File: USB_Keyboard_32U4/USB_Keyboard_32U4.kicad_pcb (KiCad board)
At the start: 2 copper layers, 13.4 x 24.2 mm, 12 parts, among them J1 USB_C_Receptacle_USB2.0_16P, U1 ATmega32U4-A, Y1 16mhz

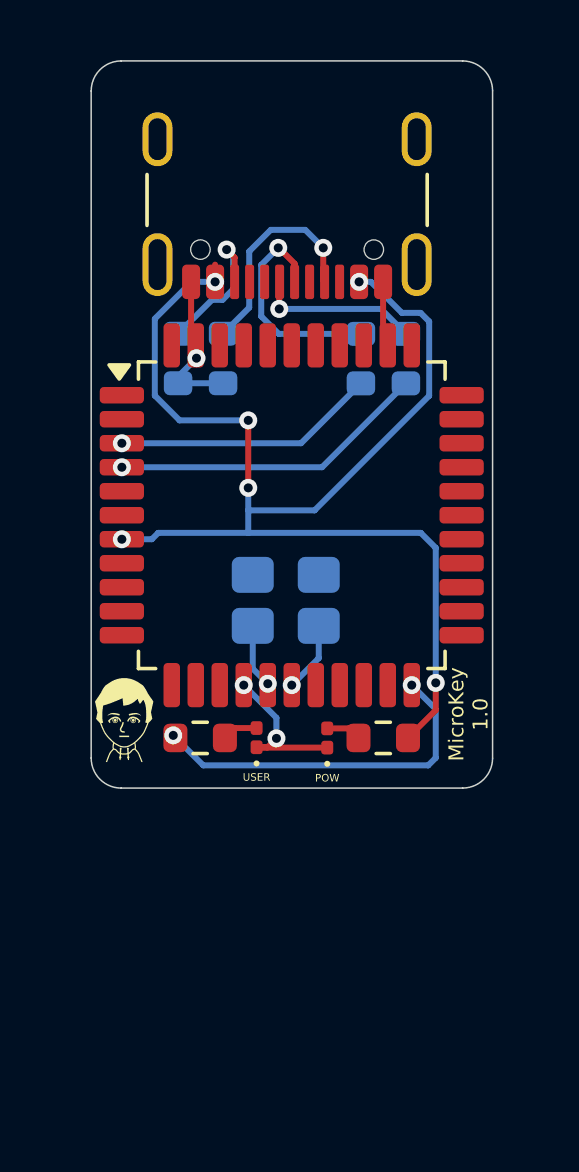
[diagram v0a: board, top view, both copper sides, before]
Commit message: Update keyboard PCB footprints to 0805
This commit updates the USB keyboard board from 0201/0603 passive packages to 0805 hand-solder footprints for the LEDs and resistors. It repositions the affected components, refreshes the KiCad project metadata, and adjusts the board outline and routed tracks to match the larger parts. It also includes the generated production .DS_Store artifact.
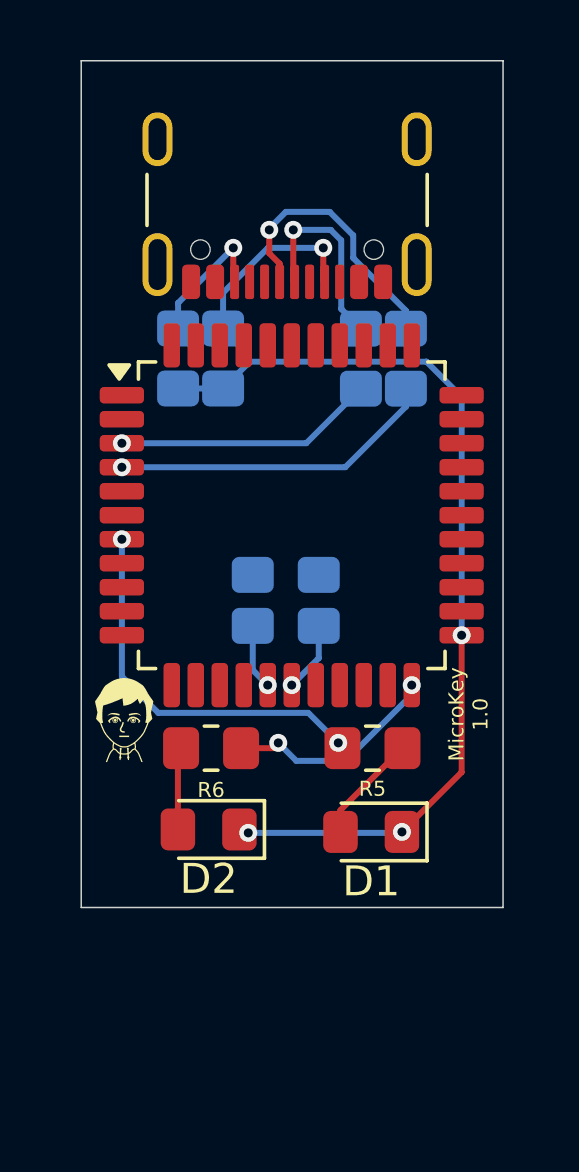
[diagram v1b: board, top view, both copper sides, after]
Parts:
- D1: renamed from POW; value LED -> RED; footprint LED_SMD:LED_0201_0603Metric -> LED_SMD:LED_0805_2012Metric_Pad1.15x1.40mm_HandSolder
- D2: renamed from USER; value LED -> BLUE; footprint LED_SMD:LED_0201_0603Metric -> LED_SMD:LED_0805_2012Metric_Pad1.15x1.40mm_HandSolder
- R1, R2, R3, R4, R5, R6: footprint Resistor_SMD:R_0603_1608Metric -> Resistor_SMD:R_0805_2012Metric_Pad1.20x1.40mm_HandSolder
- moved D1 3.46 mm to (122.6, 92.0), turned to 180 degrees
- moved D2 3.45 mm to (117.2, 91.9), turned to 180 degrees
- moved R6 0.50 mm to (117.3, 89.2), turned to 180 degrees
- moved R5 0.50 mm to (122.6, 89.2), turned to 180 degrees
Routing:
- net Net-(U1-VBUS): track 43.8 -> 12.9 mm, vias 6 -> 2
- net /Net-(J1-GND-PadA1): track 12.3 -> 31.6 mm
- net /unconnected-(U1-PD5-Pad22): track 12.1 -> 7.68 mm
- net Net-(J1-D--PadA7): track 5.48 -> 9.11 mm
- net Net-(D1-A): track 1.17 -> 3.65 mm
- net Net-(D2-A): track 1.40 -> 2.75 mm
- net Net-(J1-CC1): track 7.27 -> 6.30 mm
- net Net-(J1-D+-PadA6): track 7.45 -> 6.71 mm
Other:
- board size 13.4 x 24.2 mm -> 14.1 x 28.2 mm

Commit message: edited the dimensions of the cutout
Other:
- board size 14.1 x 28.2 mm -> 15 x 30 mm
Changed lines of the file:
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@@
 	)
 	(gr_rect
-		(start 112.932449 66.262724)
-		(end 126.993325 94.487757)
+		(start 112.25 66.262724)
+		(end 127.25 96.262724)
 		(stroke
 			(width 0.05)

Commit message: Edited some pcb layout
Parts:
- added J2: Conn_02x03_Odd_Even, Connector_PinHeader_2.54mm:PinHeader_2x03_P2.54mm_Vertical, F.Cu at (117.4, 98.8)
- added R7: R, Resistor_SMD:R_0805_2012Metric_Pad1.20x1.40mm_HandSolder, B.Cu at (119.5, 91.6)
- moved D2 1.01 mm to (117.8, 91.1)
- moved D1 0.75 mm to (122.4, 91.3)
- moved R6 0.66 mm to (117.9, 89.1)
- moved R5 0.23 mm to (122.4, 89.2)
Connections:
- U1 pad 10: unconnected-(U1-PB2-Pad10) -> Net-(J2-Pin_3)
- U1 pad 11: unconnected-(U1-PB3-Pad11) -> Net-(J2-Pin_4)
- U1 pad 32: unconnected-(U1-PC7-Pad32) -> Net-(J2-Pin_6)
- U1 pad 9: unconnected-(U1-PB1-Pad9) -> Net-(J2-Pin_5)
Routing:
- net Net-(U1-VBUS): track 12.9 -> 41.2 mm, vias 2 -> 4
- net Net-(J2-Pin_5): track 0.00 -> 21.3 mm, vias 0 -> 2
- net Net-(J2-Pin_3): track 0.00 -> 20.9 mm, vias 0 -> 2
- net Net-(U1-AVCC-Pad24): track 0.00 -> 13.7 mm
- net Net-(J2-Pin_4): track 0.00 -> 13.2 mm, vias 0 -> 1
- net Net-(J2-Pin_2): track 0.00 -> 10.9 mm, vias 0 -> 1
- net Net-(J2-Pin_6): track 0.00 -> 4.86 mm
- net /Net-(J1-GND-PadA1): track 31.6 -> 36.2 mm, vias 3 -> 1
- net Net-(J1-CC2): track 4.60 -> 8.97 mm
- net Net-(J1-D+-PadA6): track 6.71 -> 4.38 mm
- net Net-(J1-CC1): track 6.30 -> 8.50 mm
- net Net-(J1-D--PadA7): track 9.11 -> 7.62 mm
- net /unconnected-(U1-PD5-Pad22): track 7.68 -> 6.64 mm, vias 2 -> 0
- net Net-(D2-A): track 2.75 -> 2.01 mm
- net Net-(D1-A): track 3.65 -> 2.93 mm
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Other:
- board size 15 x 30 mm -> 15 x 35 mm
- board text removed: "R4"
